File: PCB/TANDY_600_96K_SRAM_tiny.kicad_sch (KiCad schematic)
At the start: 5 parts, among them J1 DIN-41612-44-M-RA, U1 628128, U2 74HC148

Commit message: add tiny version
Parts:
- C1, C2: footprint 000_LOCAL:C_1206 -> 000_LOCAL:C_0805
- J1: value DIN-41612-44-M-RA -> DIN41612-44-mounts; symbol 000_LOCAL:DIN41612-44 -> 000_LOCAL:DIN41612-44-mounts
- U1: value 628128 -> 628128_TSOP32; footprint 000_LOCAL:SOP-32W -> 000_LOCAL:TSOP32-dual; symbol 000_LOCAL:628128_DIP32_SSOP32 -> 000_LOCAL:628128_TSOP32
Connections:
- net A0: now also U1.20 (A0); no longer U1.12 (A0)
- net A1: now also U1.19 (A1); no longer U1.11 (A1)
- net A10: now also U1.31 (A10); no longer U1.23 (A10)
- net A11: now also U1.1 (A11); no longer U1.25 (A11)
- net A12: now also U1.12 (A12); no longer U1.4 (A12)
- net A13: now also U1.4 (A13); no longer U1.28 (A13)
- net A14: now also U1.11 (A14); no longer U1.3 (A14)
- net A15: now also U1.7 (A15); no longer U1.31 (A15)
- net A16: now also U1.10 (A16); no longer U1.2 (A16)
- net A2: now also U1.18 (A2); no longer U1.10 (A2)
- net A3: now also U1.17 (A3); no longer U1.9 (A3)
- net A4: now also U1.16 (A4); no longer U1.8 (A4)
- net A5: now also U1.15 (A5); no longer U1.7 (A5)
- net A6: now also U1.14 (A6); no longer U1.6 (A6)
- net A7: now also U1.13 (A7); no longer U1.5 (A7)
- net A8: now also U1.3 (A8); no longer U1.27 (A8)
- net A9: now also U1.2 (A9); no longer U1.26 (A9)
- net CS2: now also U1.6 (CS2); no longer U1.30 (CS2)
- net D0: now also U1.21 (Q0); no longer U1.13 (Q0)
- net D1: now also U1.22 (Q1); no longer U1.14 (Q1)
- net D2: now also U1.23 (Q2); no longer U1.15 (Q2)
- net D3: now also U1.25 (Q3); no longer U1.17 (Q3)
- net D4: now also U1.26 (Q4); no longer U1.18 (Q4)
- net D5: now also U1.27 (Q5); no longer U1.19 (Q5)
- net D6: now also U1.28 (Q6); no longer U1.20 (Q6)
- net D7: now also U1.29 (Q7); no longer U1.21 (Q7)
- net GND: now also J1.S (mount_holes), U1.24 (GND); no longer U1.16 (GND)
- net VMEM: now also U1.8 (VCC); no longer U1.32 (VCC)
- net ~{CS1}: now also U1.30 (~{CS1}); no longer U1.22 (~{CS1})
- net ~{OE}: now also U1.32 (~{OE}); no longer U1.24 (~{OE})
- net ~{WE}: now also U1.5 (~{WE}); no longer U1.29 (~{WE})
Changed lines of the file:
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@@
       (effects (font (size 1.27 1.27)) (justify left))
     )
-    (property "Footprint" "000_LOCAL:C_1206" (id 2) (at 207.9752 53.34 0)
+    (property "Footprint" "000_LOCAL:C_0805" (id 2) (at 207.9752 53.34 0)
       (effects (font (size 1.27 1.27)) hide)
     )
@@
       (effects (font (size 1.27 1.27)) (justify left))
     )
-    (property "Footprint" "000_LOCAL:C_1206" (id 2) (at 138.1252 53.34 0)
+    (property "Footprint" "000_LOCAL:C_0805" (id 2) (at 138.1252 53.34 0)
       (effects (font (size 1.27 1.27)) hide)
     )
@@
     (pin "2")
   )
-  (symbol (lib_id "000_LOCAL:DIN41612-44") (at 71.12 76.2 0) (unit 1)
+  (symbol (lib_id "000_LOCAL:DIN41612-44-mounts") (at 71.12 76.2 0) (unit 1)
     (in_bom yes) (on_board yes)
     (property "Reference" "J1" (id 0) (at 72.39 44.45 0))
-    (property "Value" "DIN-41612-44-M-RA" (id 1) (at 72.39 46.99 0))
+    (property "Value" "DIN41612-44-mounts" (id 1) (at 72.39 106.68 0))
     (property "Footprint" "000_LOCAL:DIN41612-44P-male-horiz" (id 2) (at 71.12 76.2 0)
       (effects (font (size 1.27 1.27)) hide)
@@
     (pin "9A")
     (pin "9B")
+    (pin "S")
   )
   (symbol (lib_id "000_LOCAL:VCC") (at 137.16 45.72 0) (unit 1)
@@
     (pin "1")
   )
-  (symbol (lib_id "000_LOCAL:628128_DIP32_SSOP32") (at 180.34 73.66 0) (unit 1)
+  (symbol (lib_id "000_LOCAL:628128_TSOP32") (at 180.34 73.66 0) (unit 1)
     (in_bom yes) (on_board yes)
     (property "Reference" "U1" (id 0) (at 186.055 46.863 0))
-    (property "Value" "628128" (id 1) (at 186.182 48.895 0))
-    (property "Footprint" "000_LOCAL:SOP-32W" (id 2) (at 180.34 73.66 0)
+    (property "Value" "628128_TSOP32" (id 1) (at 182.88 50.165 0)
+      (effects (font (size 1.27 1.27)) (justify left bottom))
+    )
+    (property "Footprint" "000_LOCAL:TSOP32-dual" (id 2) (at 180.34 73.66 0)
       (effects (font (size 1.27 1.27)) hide)
     )
@@
       (effects (font (size 1.27 1.27)) hide)
     )
-    (pin "16")
-    (pin "32")
+    (pin "24")
+    (pin "8")
     (pin "1")
     (pin "10")
@@
     (pin "14")
     (pin "15")
+    (pin "16")
     (pin "17")
     (pin "18")
@@
     (pin "22")
     (pin "23")
-    (pin "24")
     (pin "25")
     (pin "26")
@@
     (pin "30")
     (pin "31")
+    (pin "32")
     (pin "4")
     (pin "5")
     (pin "6")
     (pin "7")
-    (pin "8")
     (pin "9")
   )
@@
     )
     (property "Datasheet" "" (id 3) (at 180.34 99.06 0)
+      (effects (font (size 1.27 1.27)) hide)
+    )
+    (pin "1")
+  )
+  (symbol (lib_id "000_LOCAL:GND") (at 72.644 105.41 0) (unit 1)
+    (in_bom yes) (on_board yes) (fields_autoplaced)
+    (property "Reference" "#PWR0128" (id 0) (at 72.644 111.76 0)
+      (effects (font (size 1.27 1.27)) hide)
+    )
+    (property "Value" "GND" (id 1) (at 72.644 110.49 0))
+    (property "Footprint" "" (id 2) (at 72.644 105.41 0)
+      (effects (font (size 1.27 1.27)) hide)
+    )
+    (property "Datasheet" "" (id 3) (at 72.644 105.41 0)
       (effects (font (size 1.27 1.27)) hide)
     )
@@
       (reference "#PWR0127") (unit 1) (value "GND") (footprint "")
     )
+    (path "/131f54b5-f88e-4a42-a08d-1d241e188393"
+      (reference "#PWR0128") (unit 1) (value "GND") (footprint "")
+    )
     (path "/00000000-0000-0000-0000-0000586e7dab"
-      (reference "C1") (unit 1) (value "0.1uF") (footprint "000_LOCAL:C_1206")
+      (reference "C1") (unit 1) (value "0.1uF") (footprint "000_LOCAL:C_0805")
     )
     (path "/00000000-0000-0000-0000-0000587f7a69"
-      (reference "C2") (unit 1) (value "0.1uF") (footprint "000_LOCAL:C_1206")
+      (reference "C2") (unit 1) (value "0.1uF") (footprint "000_LOCAL:C_0805")
     )
     (path "/00000000-0000-0000-0000-000061163f2f"
-      (reference "J1") (unit 1) (value "DIN-41612-44-M-RA") (footprint "000_LOCAL:DIN41612-44P-male-horiz")
+      (reference "J1") (unit 1) (value "DIN41612-44-mounts") (footprint "000_LOCAL:DIN41612-44P-male-horiz")
     )
     (path "/00000000-0000-0000-0000-0000613c8a04"
-      (reference "U1") (unit 1) (value "628128") (footprint "000_LOCAL:SOP-32W")
+      (reference "U1") (unit 1) (value "628128_TSOP32") (footprint "000_LOCAL:TSOP32-dual")
     )
     (path "/00000000-0000-0000-0000-0000613445a6"

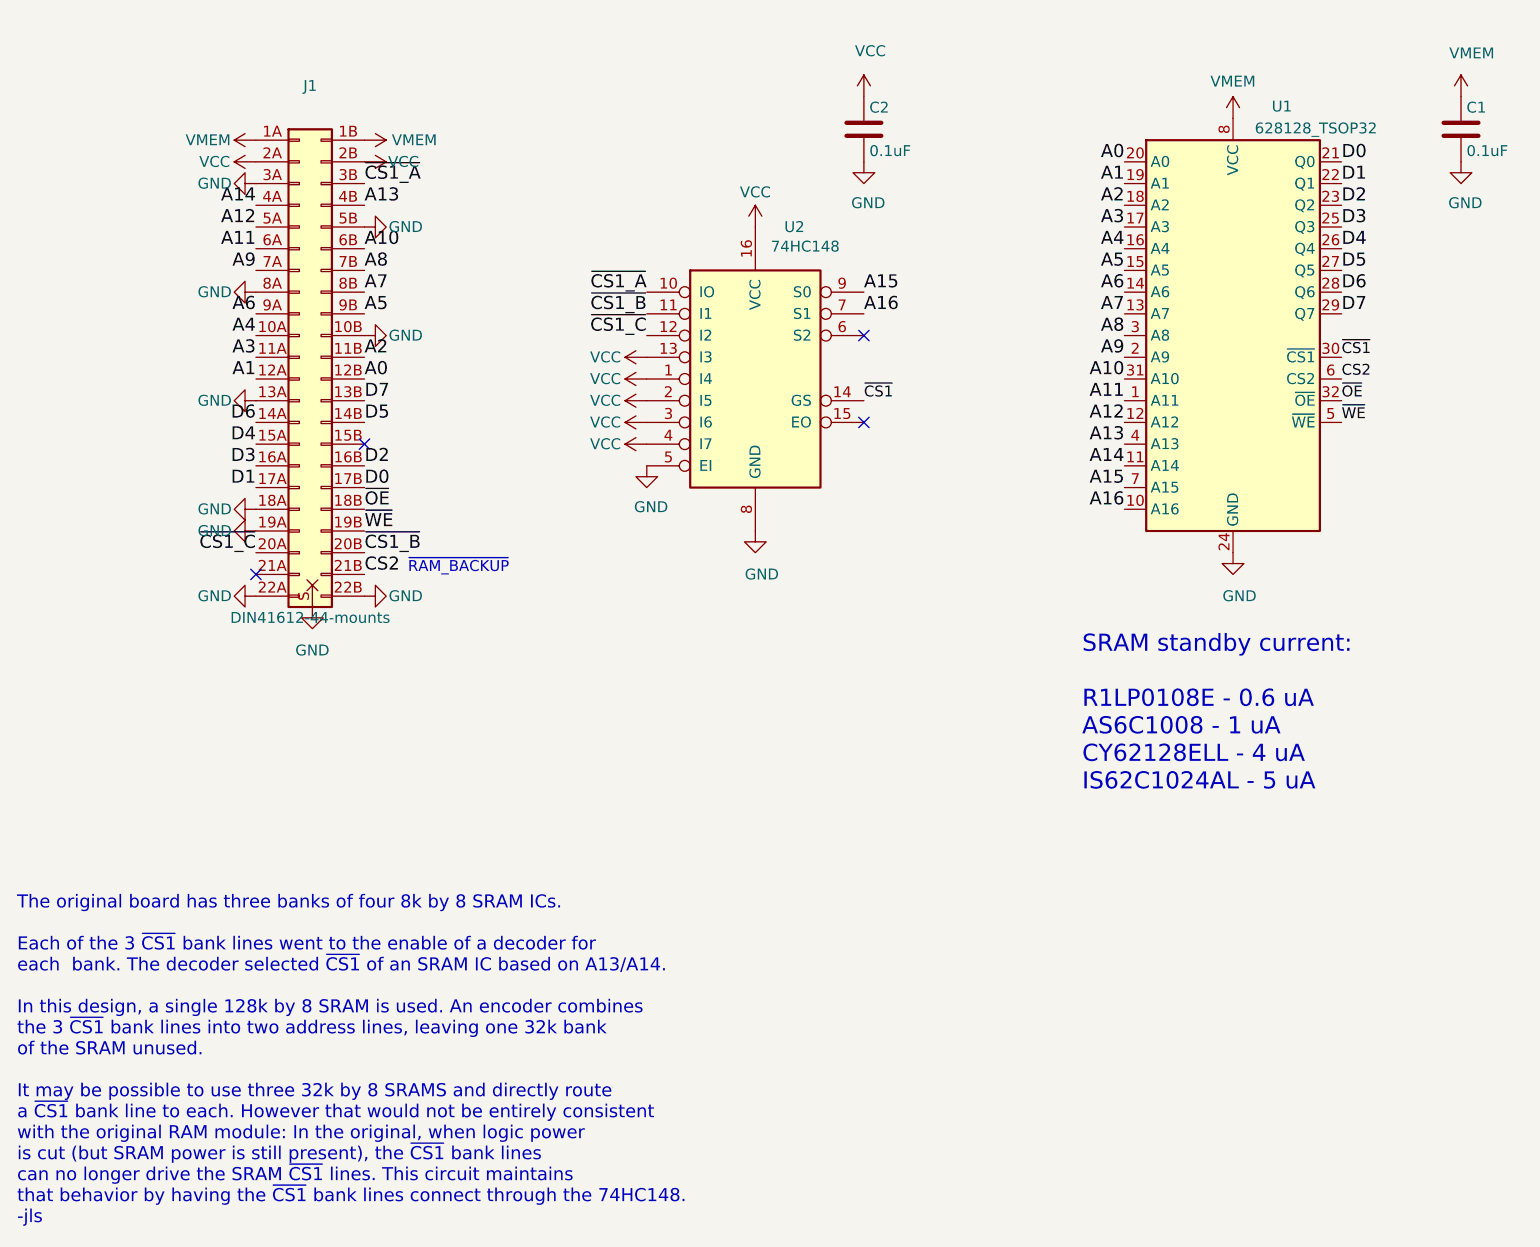
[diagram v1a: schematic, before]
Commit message: silkscreen, symbols, footprints touchups
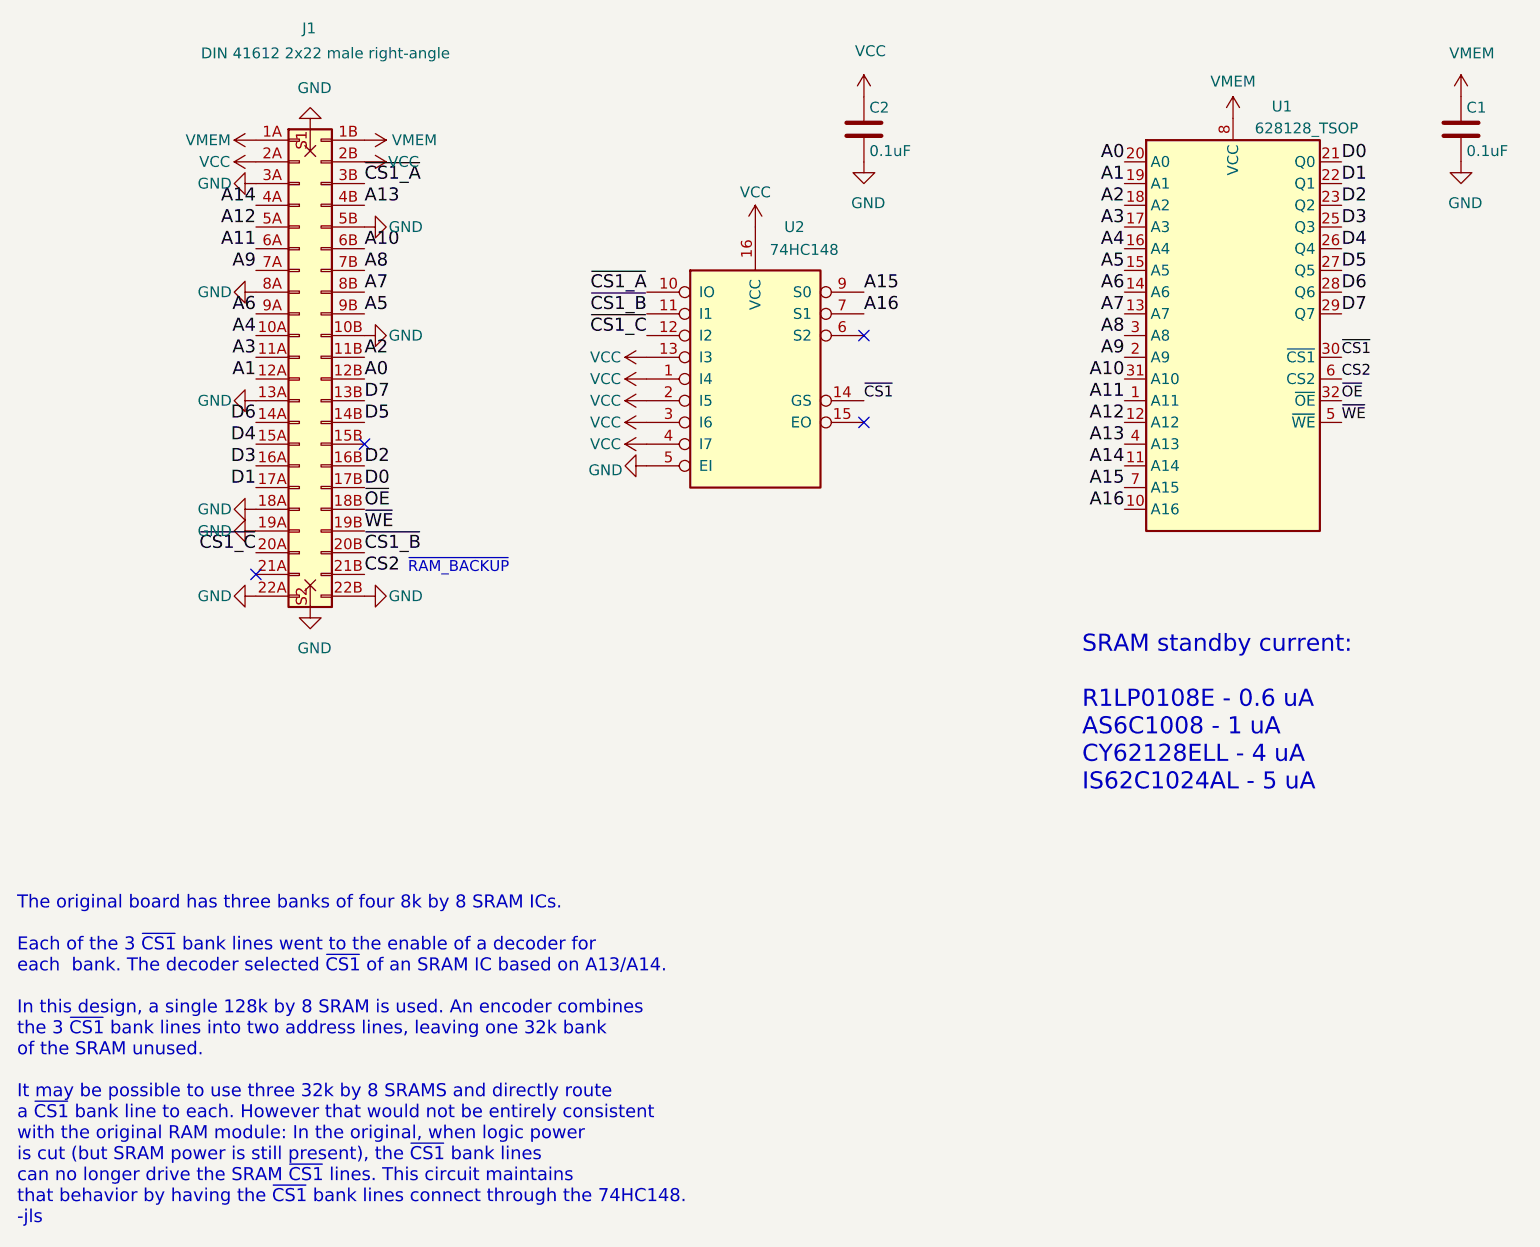
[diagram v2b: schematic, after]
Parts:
- J1: value DIN41612-44-mounts -> DIN 41612 2x22 male right-angle; footprint 000_LOCAL:DIN41612-44P-male-horiz -> 000_LOCAL:DIN 41612 2x22 male right-angle; symbol 000_LOCAL:DIN41612-44-mounts -> 000_LOCAL:DIN 41612 2x22 male right-angle
- U1: value 628128_TSOP32 -> 628128_TSOP; symbol 000_LOCAL:628128_TSOP32 -> 000_LOCAL:628128_TSOP
- U2: footprint 000_LOCAL:SOIC-SOP-16 -> (none)
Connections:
- net GND: now also J1.S1 (mount), J1.S2 (mount); no longer J1.S (mount_holes)
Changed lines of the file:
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@@
     (pin "2")
   )
-  (symbol (lib_id "000_LOCAL:DIN41612-44-mounts") (at 71.12 76.2 0) (unit 1)
-    (in_bom yes) (on_board yes)
-    (property "Reference" "J1" (id 0) (at 72.39 44.45 0))
-    (property "Value" "DIN41612-44-mounts" (id 1) (at 72.39 106.68 0))
-    (property "Footprint" "000_LOCAL:DIN41612-44P-male-horiz" (id 2) (at 71.12 76.2 0)
+  (symbol (lib_id "000_LOCAL:DIN 41612 2x22 male right-angle") (at 71.12 76.2 0) (unit 1)
+    (in_bom yes) (on_board yes)
+    (property "Reference" "J1" (id 0) (at 72.263 37.719 0))
+    (property "Value" "DIN 41612 2x22 male right-angle" (id 1) (at 74.168 40.64 0))
+    (property "Footprint" "000_LOCAL:DIN 41612 2x22 male right-angle" (id 2) (at 71.12 76.2 0)
       (effects (font (size 1.27 1.27)) hide)
     )
@@
     (pin "9A")
     (pin "9B")
-    (pin "S")
+    (pin "S1")
+    (pin "S2")
   )
   (symbol (lib_id "000_LOCAL:VCC") (at 137.16 45.72 0) (unit 1)
@@
     (pin "1")
   )
-  (symbol (lib_id "000_LOCAL:GND") (at 111.76 88.9 0) (unit 1)
-    (in_bom yes) (on_board yes)
-    (property "Reference" "#PWR0114" (id 0) (at 111.76 95.25 0)
-      (effects (font (size 1.27 1.27)) hide)
-    )
-    (property "Value" "GND" (id 1) (at 112.268 93.726 0))
+  (symbol (lib_id "000_LOCAL:GND") (at 111.76 88.9 270) (unit 1)
+    (in_bom yes) (on_board yes)
+    (property "Reference" "#PWR0114" (id 0) (at 105.41 88.9 0)
+      (effects (font (size 1.27 1.27)) hide)
+    )
+    (property "Value" "GND" (id 1) (at 106.934 89.408 90))
     (property "Footprint" "" (id 2) (at 111.76 88.9 0)
       (effects (font (size 1.27 1.27)) hide)
@@
     (in_bom yes) (on_board yes)
     (property "Reference" "U2" (id 0) (at 129.032 60.96 0))
-    (property "Value" "74HC148" (id 1) (at 130.302 63.246 0))
-    (property "Footprint" "000_LOCAL:SOIC-SOP-16" (id 2) (at 124.46 78.74 0)
+    (property "Value" "74HC148" (id 1) (at 130.175 63.627 0))
+    (property "Footprint" "" (id 2) (at 124.46 78.74 0)
       (effects (font (size 1.27 1.27)) hide)
     )
@@
     (pin "1")
   )
-  (symbol (lib_id "000_LOCAL:GND") (at 124.46 96.52 0) (unit 1)
-    (in_bom yes) (on_board yes)
-    (property "Reference" "#PWR0126" (id 0) (at 124.46 102.87 0)
-      (effects (font (size 1.27 1.27)) hide)
-    )
-    (property "Value" "GND" (id 1) (at 125.222 101.6 0))
-    (property "Footprint" "" (id 2) (at 124.46 96.52 0)
-      (effects (font (size 1.27 1.27)) hide)
-    )
-    (property "Datasheet" "" (id 3) (at 124.46 96.52 0)
-      (effects (font (size 1.27 1.27)) hide)
-    )
-    (pin "1")
-  )
-  (symbol (lib_id "000_LOCAL:628128_TSOP32") (at 180.34 73.66 0) (unit 1)
+  (symbol (lib_id "000_LOCAL:628128_TSOP") (at 180.34 73.66 0) (unit 1)
     (in_bom yes) (on_board yes)
     (property "Reference" "U1" (id 0) (at 186.055 46.863 0))
-    (property "Value" "628128_TSOP32" (id 1) (at 182.88 50.165 0)
+    (property "Value" "628128_TSOP" (id 1) (at 182.88 50.165 0)
       (effects (font (size 1.27 1.27)) (justify left bottom))
     )
@@
     (pin "9")
   )
-  (symbol (lib_id "000_LOCAL:GND") (at 180.34 99.06 0) (unit 1)
-    (in_bom yes) (on_board yes)
-    (property "Reference" "#PWR0127" (id 0) (at 180.34 105.41 0)
-      (effects (font (size 1.27 1.27)) hide)
-    )
-    (property "Value" "GND" (id 1) (at 181.102 104.14 0))
-    (property "Footprint" "" (id 2) (at 180.34 99.06 0)
-      (effects (font (size 1.27 1.27)) hide)
-    )
-    (property "Datasheet" "" (id 3) (at 180.34 99.06 0)
-      (effects (font (size 1.27 1.27)) hide)
-    )
-    (pin "1")
-  )
-  (symbol (lib_id "000_LOCAL:GND") (at 72.644 105.41 0) (unit 1)
-    (in_bom yes) (on_board yes) (fields_autoplaced)
-    (property "Reference" "#PWR0128" (id 0) (at 72.644 111.76 0)
-      (effects (font (size 1.27 1.27)) hide)
-    )
-    (property "Value" "GND" (id 1) (at 72.644 110.49 0))
-    (property "Footprint" "" (id 2) (at 72.644 105.41 0)
-      (effects (font (size 1.27 1.27)) hide)
-    )
-    (property "Datasheet" "" (id 3) (at 72.644 105.41 0)
+  (symbol (lib_id "000_LOCAL:GND") (at 72.39 105.41 0) (unit 1)
+    (in_bom yes) (on_board yes)
+    (property "Reference" "#PWR0126" (id 0) (at 72.39 111.76 0)
+      (effects (font (size 1.27 1.27)) hide)
+    )
+    (property "Value" "GND" (id 1) (at 72.898 110.236 0))
+    (property "Footprint" "" (id 2) (at 72.39 105.41 0)
+      (effects (font (size 1.27 1.27)) hide)
+    )
+    (property "Datasheet" "" (id 3) (at 72.39 105.41 0)
+      (effects (font (size 1.27 1.27)) hide)
+    )
+    (pin "1")
+  )
+  (symbol (lib_id "000_LOCAL:GND") (at 72.39 49.53 0) (mirror x) (unit 1)
+    (in_bom yes) (on_board yes)
+    (property "Reference" "#PWR0127" (id 0) (at 72.39 43.18 0)
+      (effects (font (size 1.27 1.27)) hide)
+    )
+    (property "Value" "GND" (id 1) (at 72.898 44.704 0))
+    (property "Footprint" "" (id 2) (at 72.39 49.53 0)
+      (effects (font (size 1.27 1.27)) hide)
+    )
+    (property "Datasheet" "" (id 3) (at 72.39 49.53 0)
       (effects (font (size 1.27 1.27)) hide)
     )
@@
       (reference "#PWR0125") (unit 1) (value "VCC") (footprint "")
     )
-    (path "/00000000-0000-0000-0000-0000613af808"
+    (path "/2bc054b1-e56e-439b-9d1b-d1dfe0b9cb74"
       (reference "#PWR0126") (unit 1) (value "GND") (footprint "")
     )
-    (path "/00000000-0000-0000-0000-00006143edd7"
+    (path "/3c42ef3f-4aeb-4f1a-8bab-117461e8f231"
       (reference "#PWR0127") (unit 1) (value "GND") (footprint "")
-    )
-    (path "/131f54b5-f88e-4a42-a08d-1d241e188393"
-      (reference "#PWR0128") (unit 1) (value "GND") (footprint "")
     )
     (path "/00000000-0000-0000-0000-0000586e7dab"
@@
     )
     (path "/00000000-0000-0000-0000-000061163f2f"
-      (reference "J1") (unit 1) (value "DIN41612-44-mounts") (footprint "000_LOCAL:DIN41612-44P-male-horiz")
+      (reference "J1") (unit 1) (value "DIN 41612 2x22 male right-angle") (footprint "000_LOCAL:DIN 41612 2x22 male right-angle")
     )
     (path "/00000000-0000-0000-0000-0000613c8a04"
-      (reference "U1") (unit 1) (value "628128_TSOP32") (footprint "000_LOCAL:TSOP32-dual")
+      (reference "U1") (unit 1) (value "628128_TSOP") (footprint "000_LOCAL:TSOP32-dual")
     )
     (path "/00000000-0000-0000-0000-0000613445a6"
